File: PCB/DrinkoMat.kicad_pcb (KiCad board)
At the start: 2 copper layers, 108.5 x 95 mm, 26 parts

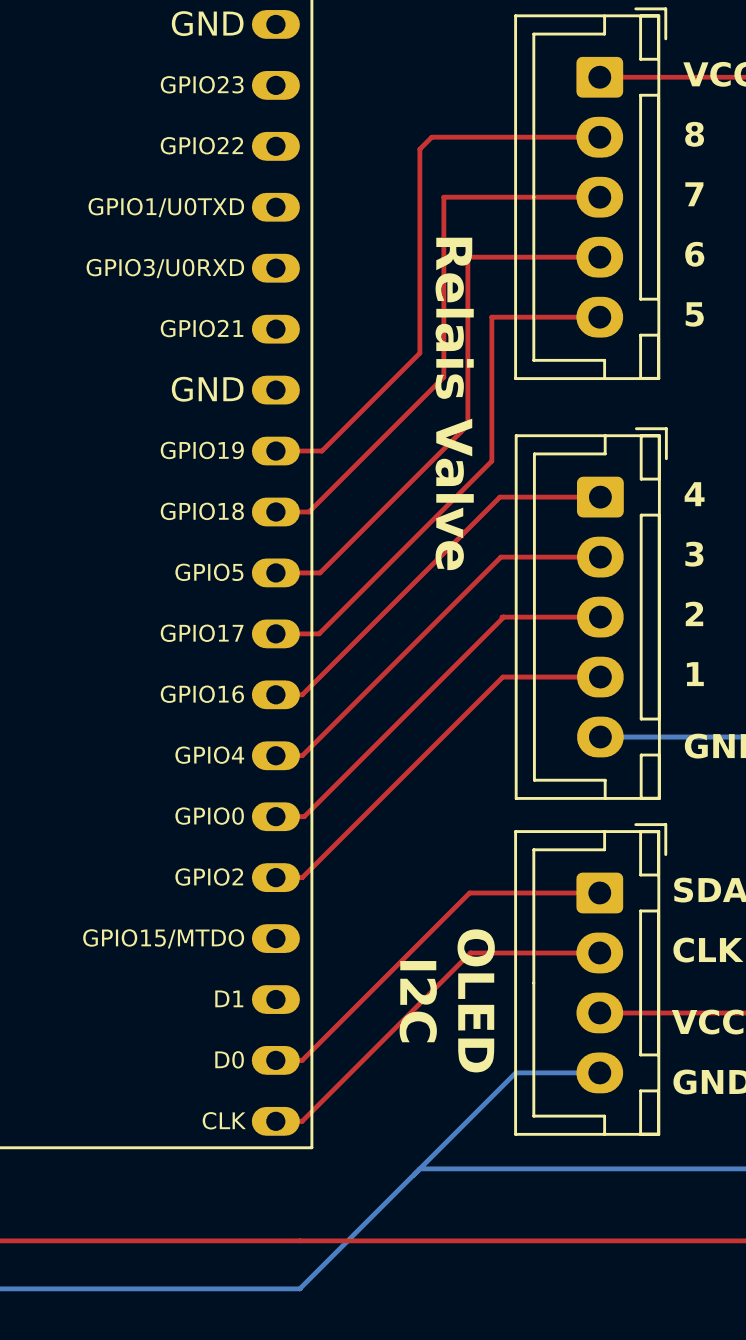
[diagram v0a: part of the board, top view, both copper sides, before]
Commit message: :sparkles: Add pin layout
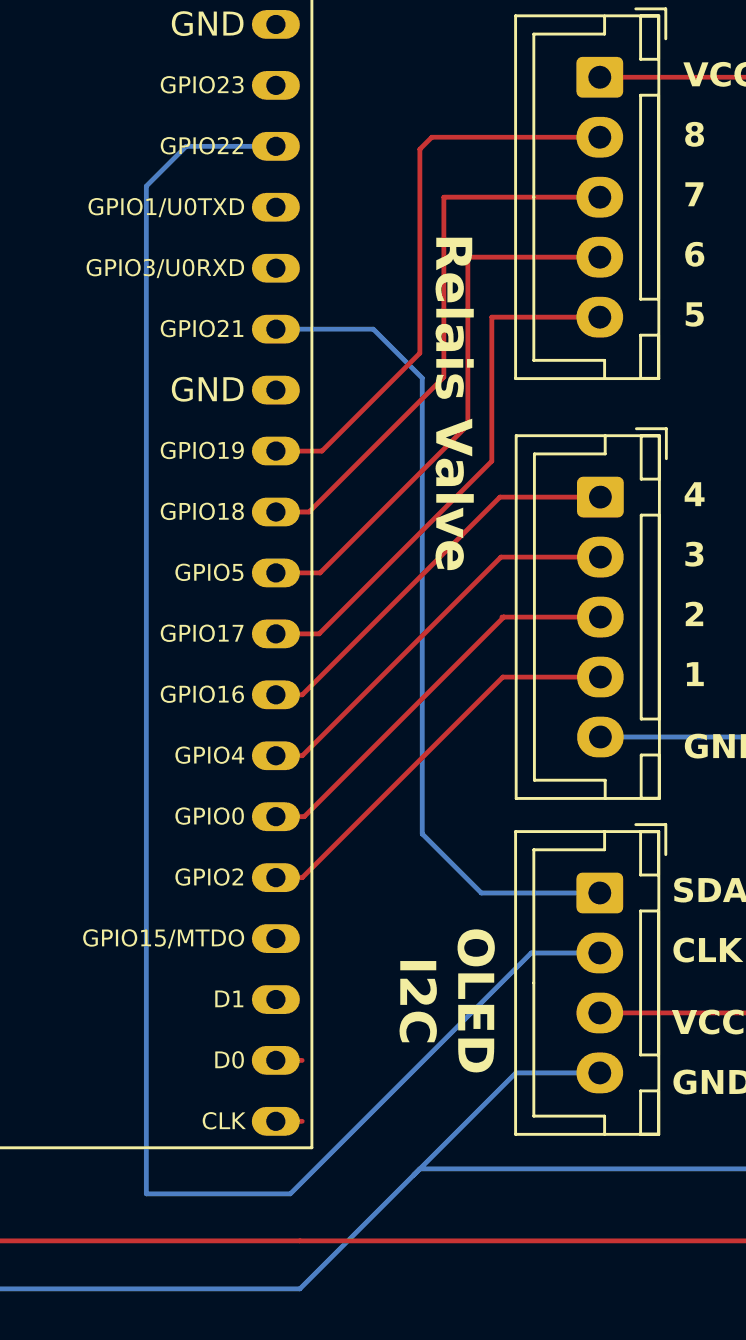
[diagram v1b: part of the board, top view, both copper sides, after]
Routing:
- net (no net): track 1167.1 -> 1242.0 mm
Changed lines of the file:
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@@
-	)
-	(segment
-		(start 82.4 58.46)
-		(end 76.9736 58.46)
-		(width 0.2)
-		(layer "F.Cu")
-		(net 0)
 	)
 	(segment
@@
 	)
 	(segment
-		(start 77.0136 60.96)
-		(end 82.4 60.96)
-		(width 0.2)
-		(layer "F.Cu")
-		(net 0)
-	)
-	(segment
 		(start 63 98.5)
 		(end 65.5 98.5)
@@
 	)
 	(segment
-		(start 76.9736 58.46)
-		(end 69.99632 65.43728)
-		(width 0.2)
-		(layer "F.Cu")
-		(net 0)
-	)
-	(segment
 		(start 82.425 46.96)
 		(end 78.4 46.96)
@@
 	)
 	(segment
-		(start 69.99632 67.97728)
-		(end 77.0136 60.96)
-		(width 0.2)
-		(layer "F.Cu")
-		(net 0)
-	)
-	(segment
 		(start 118 81.5)
 		(end 118 92)
@@
 	)
 	(segment
+		(start 79.54 60.96)
+		(end 69.5 71)
+		(width 0.2)
+		(layer "B.Cu")
+		(net 0)
+	)
+	(segment
 		(start 74.9 69.96)
 		(end 74.65 70.21)
@@
 	)
 	(segment
+		(start 63.5 71)
+		(end 63.5 29)
+		(width 0.2)
+		(layer "B.Cu")
+		(net 0)
+	)
+	(segment
 		(start 74.65 70.21)
 		(end 69.9 74.96)
@@
 	)
 	(segment
+		(start 82.4 60.96)
+		(end 79.54 60.96)
+		(width 0.2)
+		(layer "B.Cu")
+		(net 0)
+	)
+	(segment
 		(start 78.9 65.96)
 		(end 74.65 70.21)
@@
 	)
 	(segment
+		(start 75 37)
+		(end 72.96 34.96)
+		(width 0.2)
+		(layer "B.Cu")
+		(net 0)
+	)
+	(segment
 		(start 27.5 35.5)
 		(end 30 35.5)
@@
 	)
 	(segment
+		(start 63.5 29)
+		(end 65.16 27.34)
+		(width 0.2)
+		(layer "B.Cu")
+		(net 0)
+	)
+	(segment
+		(start 69.5 71)
+		(end 63.5 71)
+		(width 0.2)
+		(layer "B.Cu")
+		(net 0)
+	)
+	(segment
+		(start 65.16 27.34)
+		(end 68.9 27.34)
+		(width 0.2)
+		(layer "B.Cu")
+		(net 0)
+	)
+	(segment
+		(start 75 56)
+		(end 75 37)
+		(width 0.2)
+		(layer "B.Cu")
+		(net 0)
+	)
+	(segment
 		(start 27.5 40.5)
 		(end 27.5 35.5)
@@
 	)
 	(segment
+		(start 72.96 34.96)
+		(end 68.9 34.96)
+		(width 0.2)
+		(layer "B.Cu")
+		(net 0)
+	)
+	(segment
+		(start 77.46 58.46)
+		(end 75 56)
+		(width 0.2)
+		(layer "B.Cu")
+		(net 0)
+	)
+	(segment
 		(start 38.4 60.96)
 		(end 38.4 57.46)
@@
 		(width 0.2)
 		(layer "B.Cu")
+		(net 0)
+	)
+	(segment
+		(start 82.4 58.46)
+		(end 77.46 58.46)
+		(width 0.2)
+		(layer "B.Cu")
